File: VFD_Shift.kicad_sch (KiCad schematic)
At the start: 16 parts, among them U10 TBD62783A, U11 74HC595, U12 74HC595, U13 TBD62783A, U14 TBD62783A, U7 74HC595, U8 74HC595, U9 TBD62783A

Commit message: Add new MCU then remove original MCU and 3v3 buck converter
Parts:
- renumbered C12 to C11, C13 to C12, C14 to C13, C15 to C14, U11 to U10, U12 to U11, U13 to U12, U14 to U13, U7 to U6, U8 to U7, U9 to U8, U10 to U9

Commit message: Add in footprint for pot. and start adding some LCSC part numbers
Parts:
- VFD1, VFD2, VFD3, VFD4: LCSC Part # (none) -> -
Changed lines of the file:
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@@
       (effects (font (size 1.524 1.524)) hide)
+    )
+    (property "LCSC Part #" "-" (id 4) (at 96.52 39.37 0)
+      (effects (font (size 1.27 1.27)) hide)
     )
     (pin "1")
@@
       (effects (font (size 1.524 1.524)) hide)
     )
+    (property "LCSC Part #" "-" (id 4) (at 223.52 39.37 0)
+      (effects (font (size 1.27 1.27)) hide)
+    )
     (pin "1")
     (pin "10")
@@
     (property "Datasheet" "" (id 3) (at 223.52 111.76 0)
       (effects (font (size 1.524 1.524)) hide)
+    )
+    (property "LCSC Part #" "-" (id 4) (at 223.52 111.76 0)
+      (effects (font (size 1.27 1.27)) hide)
     )
     (pin "1")
@@
       (effects (font (size 1.524 1.524)) hide)
     )
-    (pin "1")
+    (property "LCSC Part #" "-" (id 4) (at 96.52 111.76 0)
+      (effects (font (size 1.27 1.27)) hide)
+    )
+    (pin "1")

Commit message: Added some more LCSC part numbers
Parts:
- C11, C12, C13, C14: Ext Part (none) -> N; LCSC Part # (none) -> C49678
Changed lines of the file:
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@@
+      (effects (font (size 1.27 1.27)) hide)
+    )
+    (property "Ext Part" "N" (id 4) (at 58.42 35.56 0)
+      (effects (font (size 1.27 1.27)) hide)
+    )
+    (property "LCSC Part #" "C49678" (id 5) (at 58.42 35.56 0)
       (effects (font (size 1.27 1.27)) hide)
     )
@@
       (effects (font (size 1.27 1.27)) hide)
     )
+    (property "Ext Part" "N" (id 4) (at 185.42 35.56 0)
+      (effects (font (size 1.27 1.27)) hide)
+    )
+    (property "LCSC Part #" "C49678" (id 5) (at 185.42 35.56 0)
+      (effects (font (size 1.27 1.27)) hide)
+    )
     (pin "1")
     (pin "2")
@@
       (effects (font (size 1.27 1.27)) hide)
     )
+    (property "Ext Part" "N" (id 4) (at 185.42 107.95 0)
+      (effects (font (size 1.27 1.27)) hide)
+    )
+    (property "LCSC Part #" "C49678" (id 5) (at 185.42 107.95 0)
+      (effects (font (size 1.27 1.27)) hide)
+    )
     (pin "1")
     (pin "2")
@@
       (effects (font (size 1.27 1.27)) hide)
     )
+    (property "Ext Part" "N" (id 4) (at 58.42 107.95 0)
+      (effects (font (size 1.27 1.27)) hide)
+    )
+    (property "LCSC Part #" "C49678" (id 5) (at 58.42 107.95 0)
+      (effects (font (size 1.27 1.27)) hide)
+    )

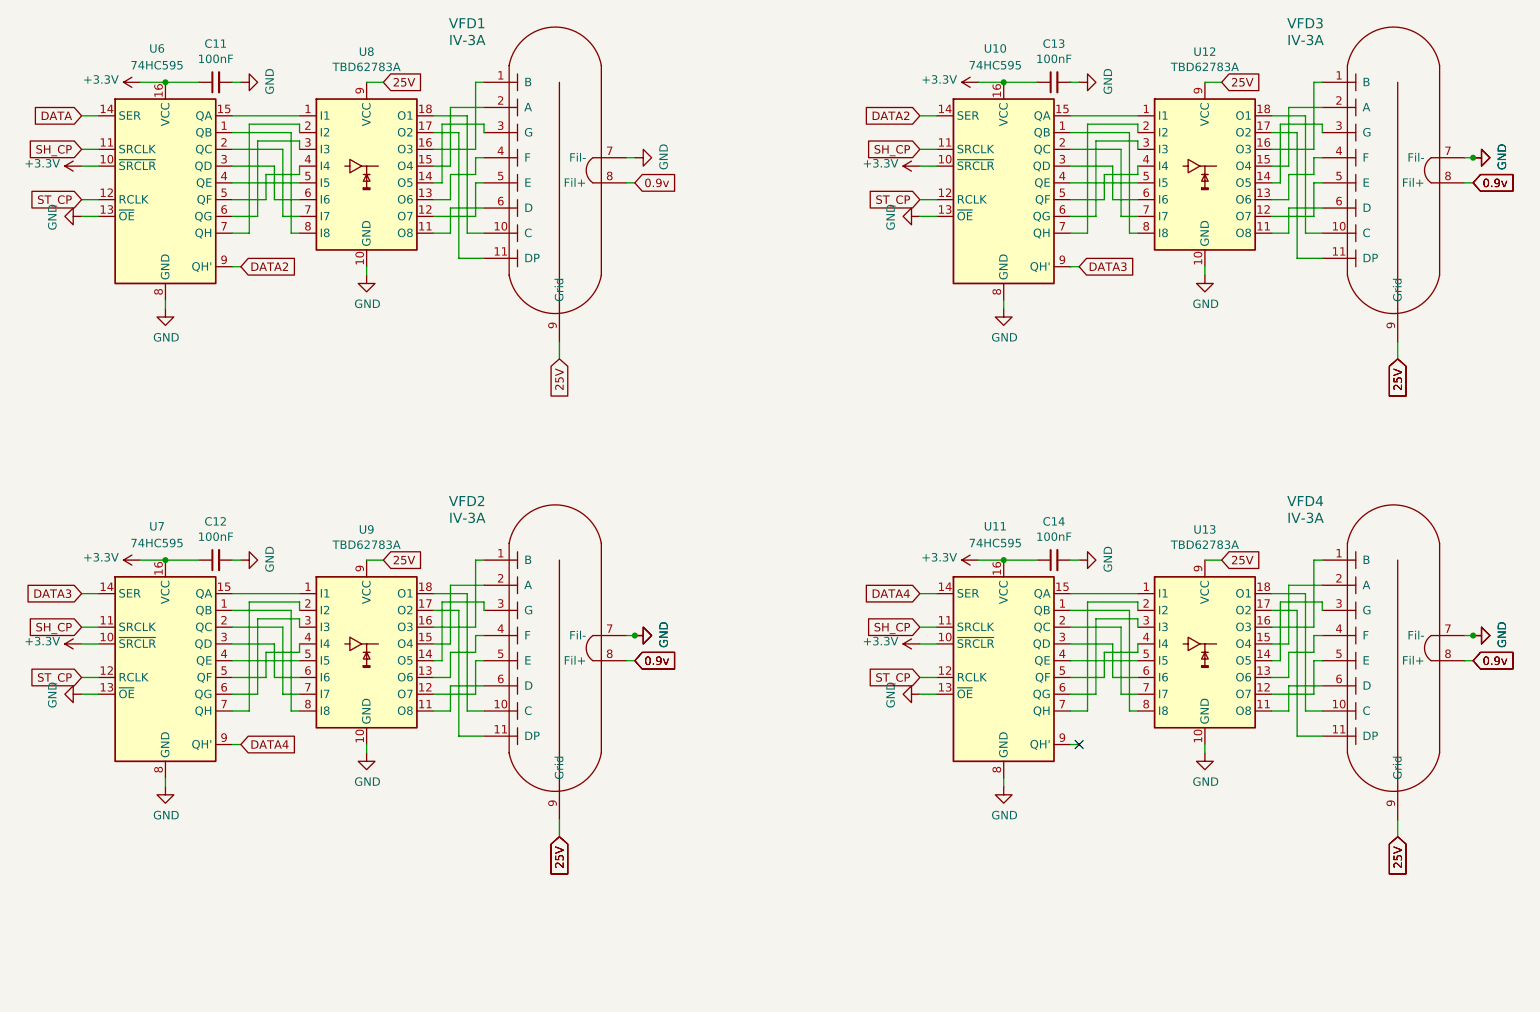
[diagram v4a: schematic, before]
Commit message: Add 100k pulldown for filament traces and add more LCSC part numbers
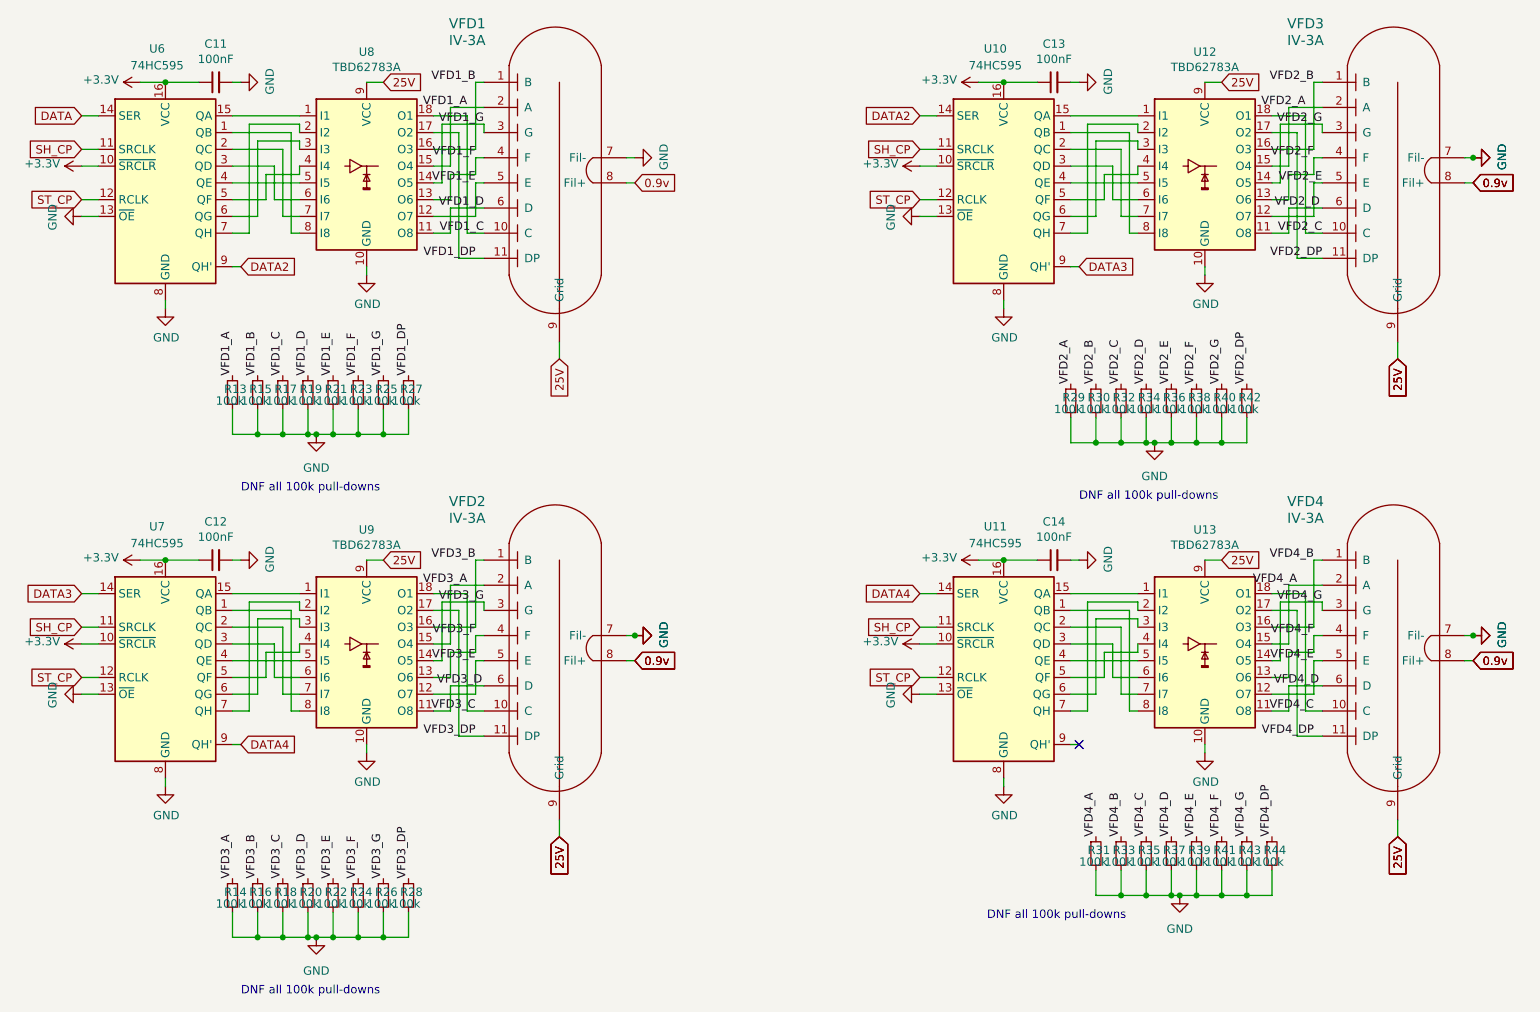
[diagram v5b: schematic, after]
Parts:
- added R13, R14, R15, R16, R17, R18, R19, R20, R21, R22, R23, R24, R25, R26, R27, R28, R29, R30, R31, R32, R33, R34, R35, R36, R37, R38, R39, R40, R41, R42, R43, R44: 100k, Resistor_SMD:R_0805_2012Metric, symbol Device:R_Small
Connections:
- net GND: now also R13.2, R14.2, R15.2, R16.2, R17.2, R18.2, R19.2, R20.2, R21.2, R22.2, R23.2, R24.2, R25.2, R26.2, R27.2, R28.2, R29.2, R30.2, R31.2, R32.2, R33.2, R34.2, R35.2, R36.2, R37.2, R38.2, R39.2, R40.2, R41.2, R42.2, R43.2, R44.2
- net VFD1_B: now reaches U8.16 (O3), VFD1.1 (B)
- net VFD1_B: now also R15.1
- net VFD1_C: now reaches U8.18 (O1), VFD1.10 (C)
- net VFD1_C: now also R17.1
- net VFD1_DP: now reaches U8.17 (O2), VFD1.11 (DP)
- net VFD1_DP: now also R27.1
- net VFD1_A: now reaches U8.15 (O4), VFD1.2 (A)
- net VFD1_A: now also R13.1
- net VFD1_G: now reaches U8.14 (O5), VFD1.3 (G)
- net VFD1_G: now also R25.1
- net VFD1_F: now reaches U8.13 (O6), VFD1.4 (F)
- net VFD1_F: now also R23.1
- net VFD1_E: now reaches U8.12 (O7), VFD1.5 (E)
- net VFD1_E: now also R21.1
- net VFD1_D: now reaches U8.11 (O8), VFD1.6 (D)
- net VFD1_D: now also R19.1
- net VFD2_B: now reaches U12.16 (O3), VFD3.1 (B)
- net VFD2_B: now also R30.1
- net VFD2_C: now reaches U12.18 (O1), VFD3.10 (C)
- net VFD2_C: now also R32.1
- net VFD2_DP: now reaches U12.17 (O2), VFD3.11 (DP)
- net VFD2_DP: now also R42.1
- net VFD2_A: now reaches U12.15 (O4), VFD3.2 (A)
- net VFD2_A: now also R29.1
- net VFD2_G: now reaches U12.14 (O5), VFD3.3 (G)
- net VFD2_G: now also R40.1
- net VFD2_F: now reaches U12.13 (O6), VFD3.4 (F)
- net VFD2_F: now also R38.1
- net VFD2_E: now reaches U12.12 (O7), VFD3.5 (E)
- net VFD2_E: now also R36.1
- net VFD2_D: now reaches U12.11 (O8), VFD3.6 (D)
- net VFD2_D: now also R34.1
- net VFD4_B: now reaches U13.16 (O3), VFD4.1 (B)
- net VFD4_B: now also R33.1
- net VFD4_C: now reaches U13.18 (O1), VFD4.10 (C)
- net VFD4_C: now also R35.1
- net VFD4_DP: now reaches U13.17 (O2), VFD4.11 (DP)
- net VFD4_DP: now also R44.1
- net VFD4_A: now reaches U13.15 (O4), VFD4.2 (A)
- net VFD4_A: now also R31.1
- net VFD4_G: now reaches U13.14 (O5), VFD4.3 (G)
- net VFD4_G: now also R43.1
- net VFD4_F: now reaches U13.13 (O6), VFD4.4 (F)
- net VFD4_F: now also R41.1
- net VFD4_E: now reaches U13.12 (O7), VFD4.5 (E)
- net VFD4_E: now also R39.1
- net VFD4_D: now reaches U13.11 (O8), VFD4.6 (D)
- net VFD4_D: now also R37.1
- net VFD3_B: now reaches U9.16 (O3), VFD2.1 (B)
- net VFD3_B: now also R16.1
- net VFD3_C: now reaches U9.18 (O1), VFD2.10 (C)
- net VFD3_C: now also R18.1
- net VFD3_DP: now reaches U9.17 (O2), VFD2.11 (DP)
- net VFD3_DP: now also R28.1
- net VFD3_A: now reaches U9.15 (O4), VFD2.2 (A)
- net VFD3_A: now also R14.1
- net VFD3_G: now reaches U9.14 (O5), VFD2.3 (G)
- net VFD3_G: now also R26.1
- net VFD3_F: now reaches U9.13 (O6), VFD2.4 (F)
- net VFD3_F: now also R24.1
- net VFD3_E: now reaches U9.12 (O7), VFD2.5 (E)
- net VFD3_E: now also R22.1
- net VFD3_D: now reaches U9.11 (O8), VFD2.6 (D)
- net VFD3_D: now also R20.1
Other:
- note added: "DNF all 100k pull-downs"
